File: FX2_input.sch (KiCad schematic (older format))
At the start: 36 parts, among them P1 CONN_10X2, P2 CONN_10X2, P3 CONN_9, P4 CONN_9

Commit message: ajout alim sur connecteur de mesure - ajout decouplage
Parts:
- removed P3, P4: CONN_9, symbol CONN_9
- added C1: 100nF, symbol C
- added P3, P4: CONN_10, symbol CONN_10
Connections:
- wire segments 76 -> 77
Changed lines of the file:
@@
 	1    0    0    -1
-$EndComp
-$Comp
-L CONN_9 P4
-U 1 1 52F2127A
-P 8750 4450
-F 0 "P4" V 8700 4450 60  0000 C CNN
-F 1 "CONN_9" V 8800 4450 60  0000 C CNN
-F 2 "" H 8750 4450 60  0000 C CNN
-F 3 "" H 8750 4450 60  0000 C CNN
-	1    8750 4450
-	1    0    0    1
-$EndComp
-$Comp
-L CONN_9 P3
-U 1 1 52F21289
-P 8750 3200
-F 0 "P3" V 8700 3200 60  0000 C CNN
-F 1 "CONN_9" V 8800 3200 60  0000 C CNN
-F 2 "" H 8750 3200 60  0000 C CNN
-F 3 "" H 8750 3200 60  0000 C CNN
-	1    8750 3200
-	1    0    0    1
 $EndComp
 Entry Bus Bus
@@
 	3300 1300 3300 3650
 Wire Bus Line
-	8000 1800 3300 1800
+	3300 1800 8300 1800
 Wire Wire Line
 	6450 1700 6450 1300
@@
 NoConn ~ 3000 3450
 NoConn ~ 2200 3450
+$Comp
+L CONN_10 P3
+U 1 1 52FC9366
+P 8750 3150
+F 0 "P3" V 8700 3150 60  0000 C CNN
+F 1 "CONN_10" V 8800 3150 60  0000 C CNN
+F 2 "" H 8750 3150 60  0000 C CNN
+F 3 "" H 8750 3150 60  0000 C CNN
+	1    8750 3150
+	1    0    0    -1
+$EndComp
+$Comp
+L CONN_10 P4
+U 1 1 52FC9375
+P 8750 4400
+F 0 "P4" V 8700 4400 60  0000 C CNN
+F 1 "CONN_10" V 8800 4400 60  0000 C CNN
+F 2 "" H 8750 4400 60  0000 C CNN
+F 3 "" H 8750 4400 60  0000 C CNN
+	1    8750 4400
+	1    0    0    -1
+$EndComp
+Entry Wire Line
+	8300 2600 8400 2700
+Entry Wire Line
+	8300 3850 8400 3950
+Text Label 8300 3850 0    60   ~ 0
+3.3v
+Text Label 8300 2600 0    60   ~ 0
+3.3v
+Wire Bus Line
+	8300 1800 8300 3850
+$Comp
+L C C1
+U 1 1 52FC9494
+P 8100 3850
+F 0 "C1" V 8150 3950 40  0000 L CNN
+F 1 "100nF" V 8250 3750 40  0000 L CNN
+F 2 "" H 8138 3700 30  0000 C CNN
+F 3 "" H 8100 3850 60  0000 C CNN
+	1    8100 3850
+	0    -1   -1   0
+$EndComp
+$Comp
+L GND #PWR1
+U 1 1 52FC94A3
+P 7900 3950
+F 0 "#PWR1" H 7900 3950 30  0001 C CNN
+F 1 "GND" H 7900 3880 30  0001 C CNN
+F 2 "" H 7900 3950 60  0000 C CNN
+F 3 "" H 7900 3950 60  0000 C CNN
+	1    7900 3950
+	1    0    0    -1
+$EndComp
+Wire Wire Line
+	7900 3850 7900 3950
 $EndSCHEMATC

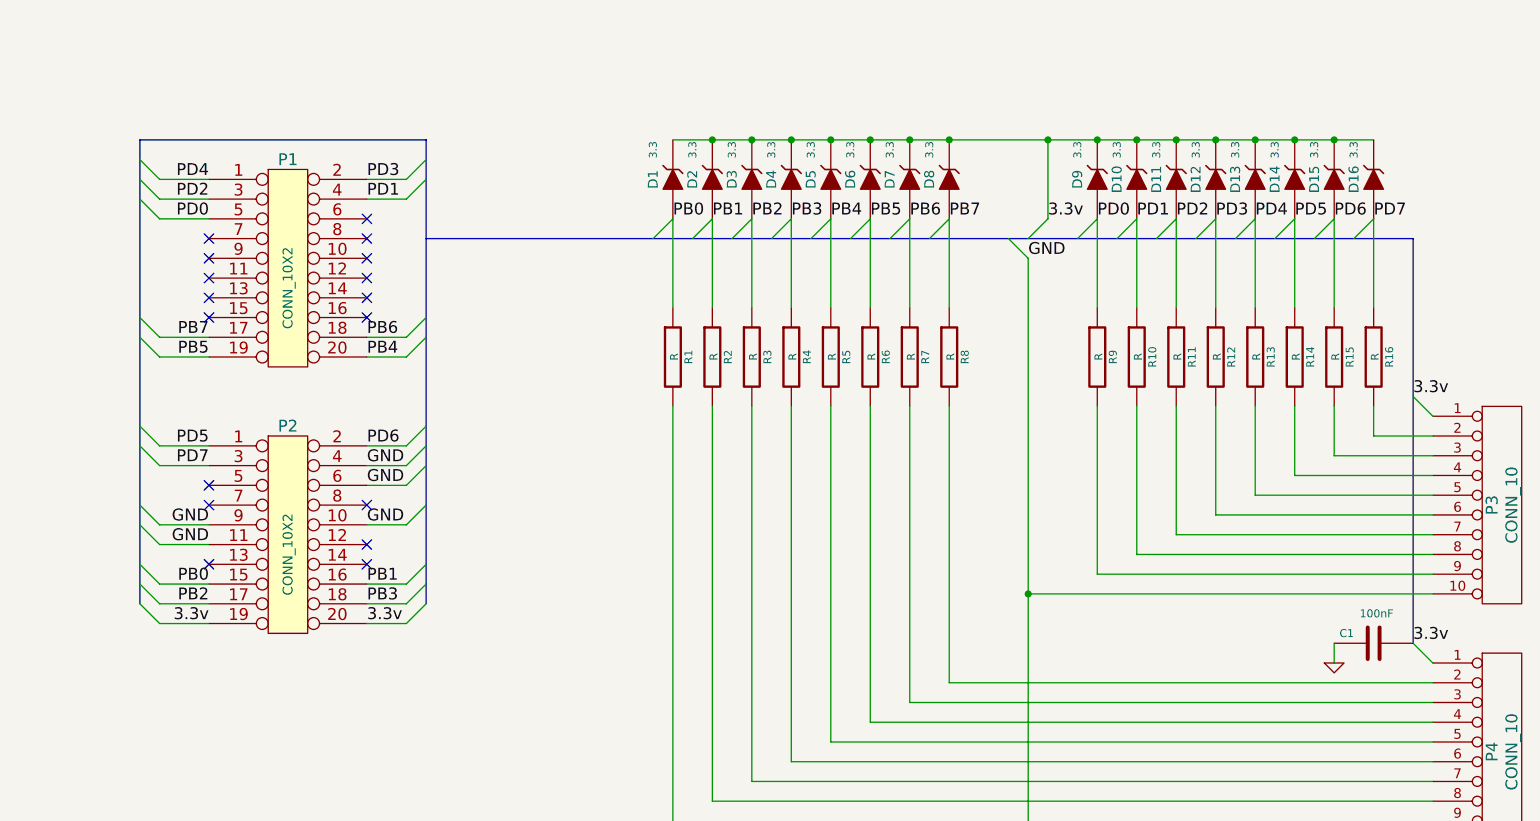
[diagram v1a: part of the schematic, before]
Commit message: new version - fit base board & power on connector
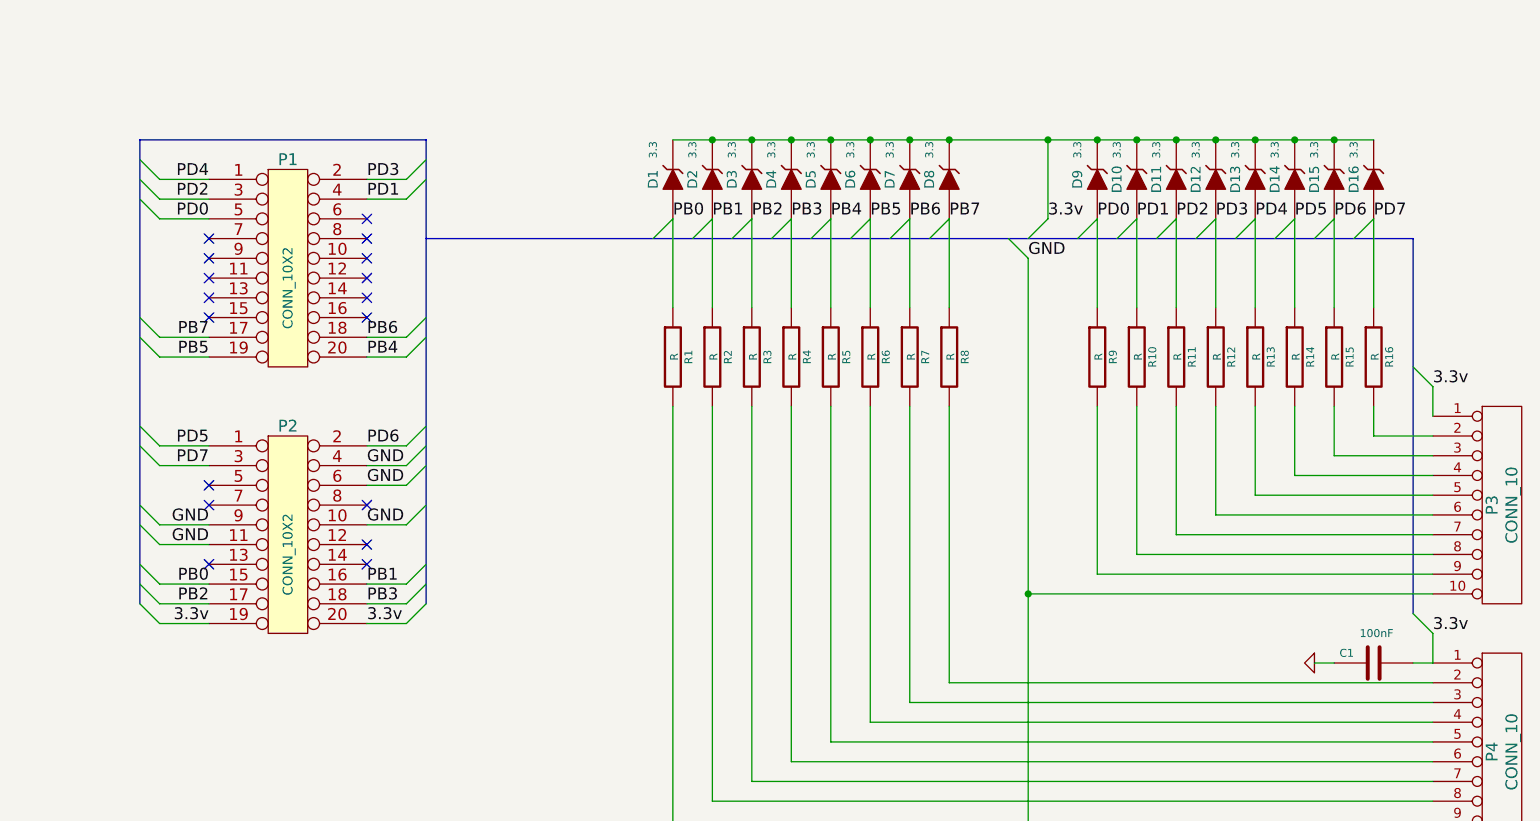
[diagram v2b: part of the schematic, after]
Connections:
- net 3.3v: now also P3.1 (P1), P4.1 (P1)
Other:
- moved on the sheet: C1
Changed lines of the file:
@@
 Connection ~ 4750 1300
 Wire Bus Line
-	1850 3650 1850 1300
+	1850 1300 1850 3650
 Wire Bus Line
 	1850 1300 3300 1300
@@
 $EndComp
 Entry Wire Line
-	8300 2600 8400 2700
-Entry Wire Line
-	8300 3850 8400 3950
-Text Label 8300 3850 0    60   ~ 0
+	8300 2450 8400 2550
+Text Label 8400 2550 0    60   ~ 0
 3.3v
-Text Label 8300 2600 0    60   ~ 0
-3.3v
-Wire Bus Line
-	8300 1800 8300 3850
 $Comp
 L C C1
 U 1 1 52FC9494
-P 8100 3850
-F 0 "C1" V 8150 3950 40  0000 L CNN
-F 1 "100nF" V 8250 3750 40  0000 L CNN
-F 2 "" H 8138 3700 30  0000 C CNN
-F 3 "" H 8100 3850 60  0000 C CNN
-	1    8100 3850
-	0    -1   -1   0
-$EndComp
-$Comp
-L GND #PWR1
+P 8100 3950
+F 0 "C1" V 8150 4050 40  0000 L CNN
+F 1 "100nF" V 8250 3850 40  0000 L CNN
+F 2 "" H 8138 3800 30  0000 C CNN
+F 3 "" H 8100 3950 60  0000 C CNN
+	1    8100 3950
+	0    -1   -1   0
+$EndComp
+$Comp
+L GND #PWR01
 U 1 1 52FC94A3
-P 7900 3950
-F 0 "#PWR1" H 7900 3950 30  0001 C CNN
-F 1 "GND" H 7900 3880 30  0001 C CNN
-F 2 "" H 7900 3950 60  0000 C CNN
-F 3 "" H 7900 3950 60  0000 C CNN
-	1    7900 3950
-	1    0    0    -1
-$EndComp
-Wire Wire Line
-	7900 3850 7900 3950
+P 7800 3950
+F 0 "#PWR01" H 7800 3950 30  0001 C CNN
+F 1 "GND" H 7800 3880 30  0001 C CNN
+F 2 "" H 7800 3950 60  0000 C CNN
+F 3 "" H 7800 3950 60  0000 C CNN
+	1    7800 3950
+	0    1    1    0
+$EndComp
+Wire Wire Line
+	8400 2550 8400 2700
+Wire Bus Line
+	8300 1800 8300 3700
+Entry Wire Line
+	8300 3700 8400 3800
+Text Label 8400 3800 0    60   ~ 0
+3.3v
+Wire Wire Line
+	8400 3800 8400 3950
+Wire Wire Line
+	8400 3950 8300 3950
+Wire Wire Line
+	7900 3950 7800 3950
 $EndSCHEMATC
